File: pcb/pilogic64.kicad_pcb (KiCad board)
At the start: 2 copper layers, 8 parts, among them SW1 RotaryEncoder_Switch, SW2 RotaryEncoder_Switch, U2 Pico

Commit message: Finished cicuit, and I think also finished pcb
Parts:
- added G***: LOGO, LOGO, F.Cu at (178.0, 36.6)
- added G***: LOGO, LOGO, F.Cu at (171.0, 149.3)
- added REF**: KiCad-Logo2_8mm_SilkScreen, Symbol:KiCad-Logo2_8mm_SilkScreen, F.Cu at (112.0, 36.0)
- added REF**: OSHW-Logo_19x20mm_SilkScreen, Symbol:OSHW-Logo_19x20mm_SilkScreen, F.Cu at (114.0, 149.3)
- added U1: ~, Connector_PinHeader_2.54mm:PinHeader_1x04_P2.54mm_Vertical, F.Cu at (139.2, 112.3)
- added U3: pam8403, Library:pam8403, F.Cu at (143.0, 150.0)
- b18650: footprint Battery:BatteryHolder_MPD_BH-18650-PC2 -> Library:18650-PC4
- moved b18650 38.3 mm to (143.0, 80.0)
- moved SD_SPI1 24.7 mm to (117.0, 45.3)
- moved TP4056-18650 24.5 mm to (163.5, 30.4)
- moved MT3608_module_SMT1 22.7 mm to (144.6, 50.3)
- moved SW1 18.9 mm to (104.5, 134.6)
- moved D1 18.7 mm to (117.5, 57.3)
- moved SW2 18.7 mm to (176.5, 134.6)
- moved U2 9.72 mm to (143.2, 127.3), turned to 90 degrees
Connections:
- U2 pad 14: unconnected-(U2-GPIO10-Pad14) -> Net-(U1-SDA)
- U2 pad 15: unconnected-(U2-GPIO11-Pad15) -> Net-(U1-SCL)
- U2 pad 19: unconnected-(U2-GPIO14-Pad19) -> Net-(U2-GPIO14)
- U2 pad 20: unconnected-(U2-GPIO15-Pad20) -> Net-(U2-GPIO15)
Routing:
- net Net-(U2-GPIO7): track 256.8 -> 0.00 mm
- net GND: track 232.8 -> 0.00 mm
- net +3.3V: track 180.0 -> 0.00 mm
- net Net-(D1-K): track 102.2 -> 0.00 mm
- net Net-(SD_SPI1-cs): track 97.6 -> 0.00 mm
- net Net-(SD_SPI1-CLK): track 95.4 -> 0.00 mm
- net Net-(SD_SPI1-MISO): track 92.6 -> 0.00 mm
- net Net-(SD_SPI1-MOSI): track 91.2 -> 0.00 mm
- net Net-(TP4056-18650-B+): track 68.4 -> 0.00 mm
- net Net-(U2-GPIO6): track 43.6 -> 0.00 mm
- net Net-(MT3608_module_SMT1-VIN-): track 26.8 -> 0.00 mm
- net Net-(U2-GPIO8): track 22.9 -> 0.00 mm
- net +5V: track 19.2 -> 0.00 mm
- net Net-(TP4056-18650-B-): track 16.5 -> 0.00 mm
- net Net-(MT3608_module_SMT1-VIN+): track 9.63 -> 0.00 mm
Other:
- board outline added: 90 x 133 mm
- board text added: "Made in Spain"
- board text added: "PiLogic64"
- board text added: "by ThePangel"

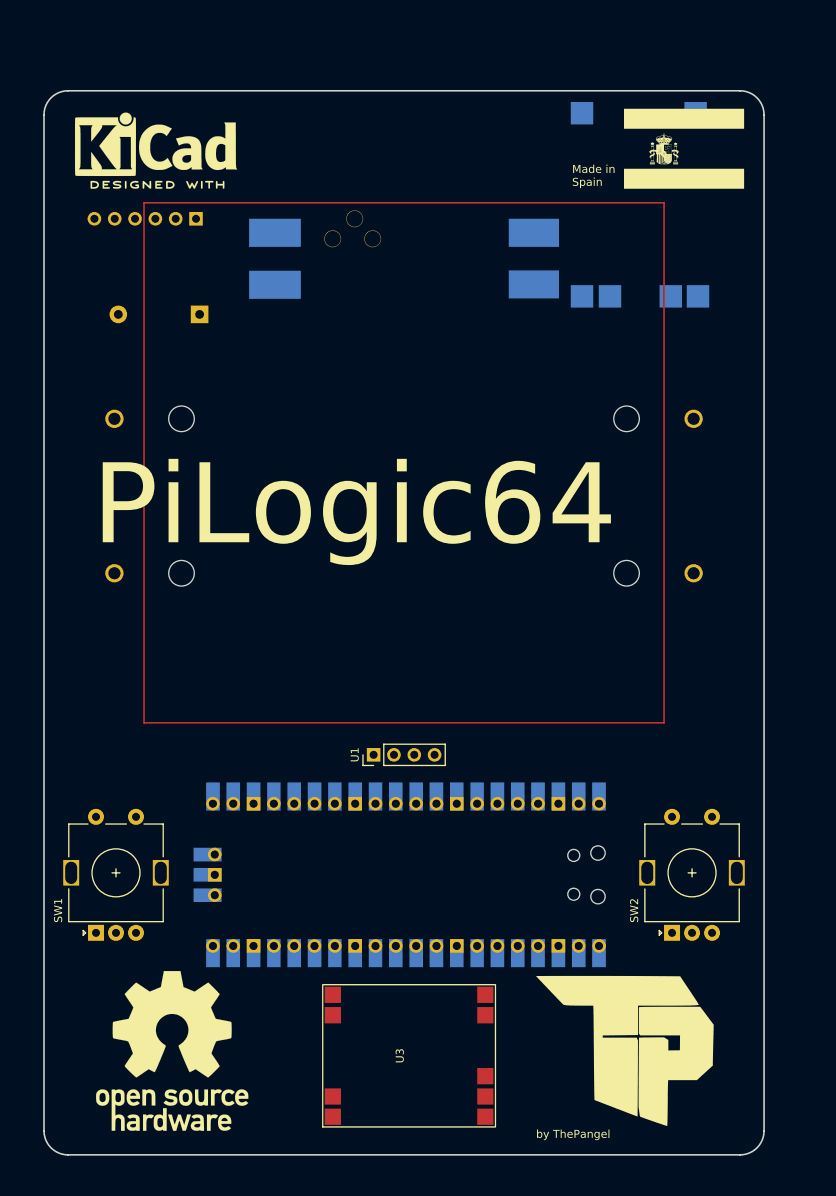
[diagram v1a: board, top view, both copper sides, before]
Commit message: added 3d models and some pcb tweaks
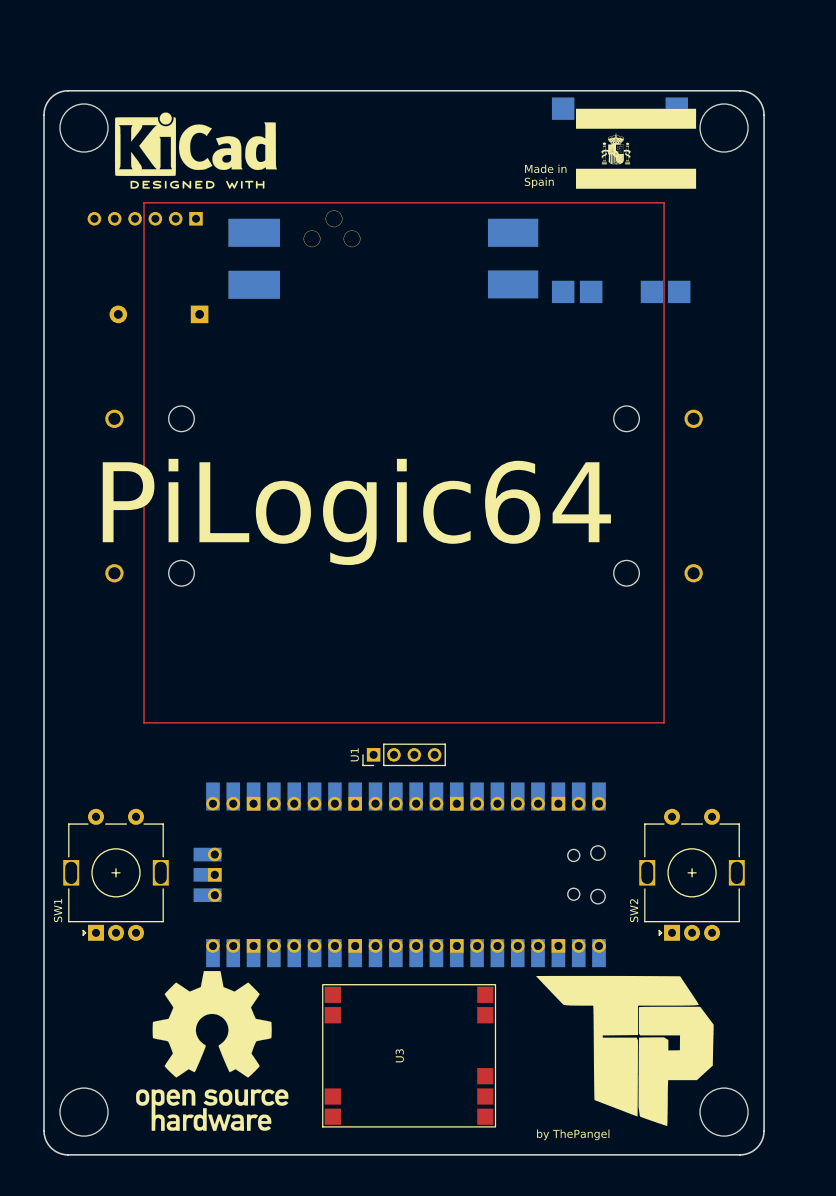
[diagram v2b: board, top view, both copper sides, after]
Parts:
- moved G*** 6.00 mm to (172.0, 36.6)
- moved REF** 5.00 mm to (117.0, 36.0)
- moved REF** 5.00 mm to (119.0, 149.3)
- moved MT3608_module_SMT1 2.59 mm to (142.0, 50.3)
- moved TP4056-18650 2.42 mm to (161.2, 29.9)
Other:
- outline, holes or cut-outs redrawn

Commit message: Finished PCB, added BOM
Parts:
- moved REF** 26.0 mm to (143.0, 34.7)
- moved SD_SPI1 5.01 mm to (115.8, 40.5), turned to 180 degrees
- moved MT3608_module_SMT1 1.15 mm to (143.0, 49.8)
- moved D1 0.70 mm to (117.5, 58.0)
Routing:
- net GND: track 0.00 -> 445.3 mm
- net +3.3V: track 0.00 -> 329.6 mm
- net +5V: track 0.00 -> 178.9 mm
- net Net-(D1-K): track 0.00 -> 125.3 mm
- net Net-(SD_SPI1-cs): track 0.00 -> 123.9 mm, vias 0 -> 1
- net Net-(SD_SPI1-MOSI): track 0.00 -> 113.9 mm, vias 0 -> 1
- net Net-(SD_SPI1-CLK): track 0.00 -> 106.3 mm, vias 0 -> 1
- net Net-(SD_SPI1-MISO): track 0.00 -> 102.1 mm, vias 0 -> 1
- net Net-(TP4056-18650-B+): track 0.00 -> 85.5 mm
- net Net-(U2-GPIO7): track 0.00 -> 58.2 mm
- net Net-(U2-GPIO9): track 0.00 -> 46.3 mm
- net Net-(U2-GPIO15): track 0.00 -> 42.9 mm
- net Net-(U2-GPIO6): track 0.00 -> 38.5 mm
- net Net-(U2-GPIO14): track 0.00 -> 38.2 mm
- net Net-(TP4056-18650-B-): track 0.00 -> 37.3 mm
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
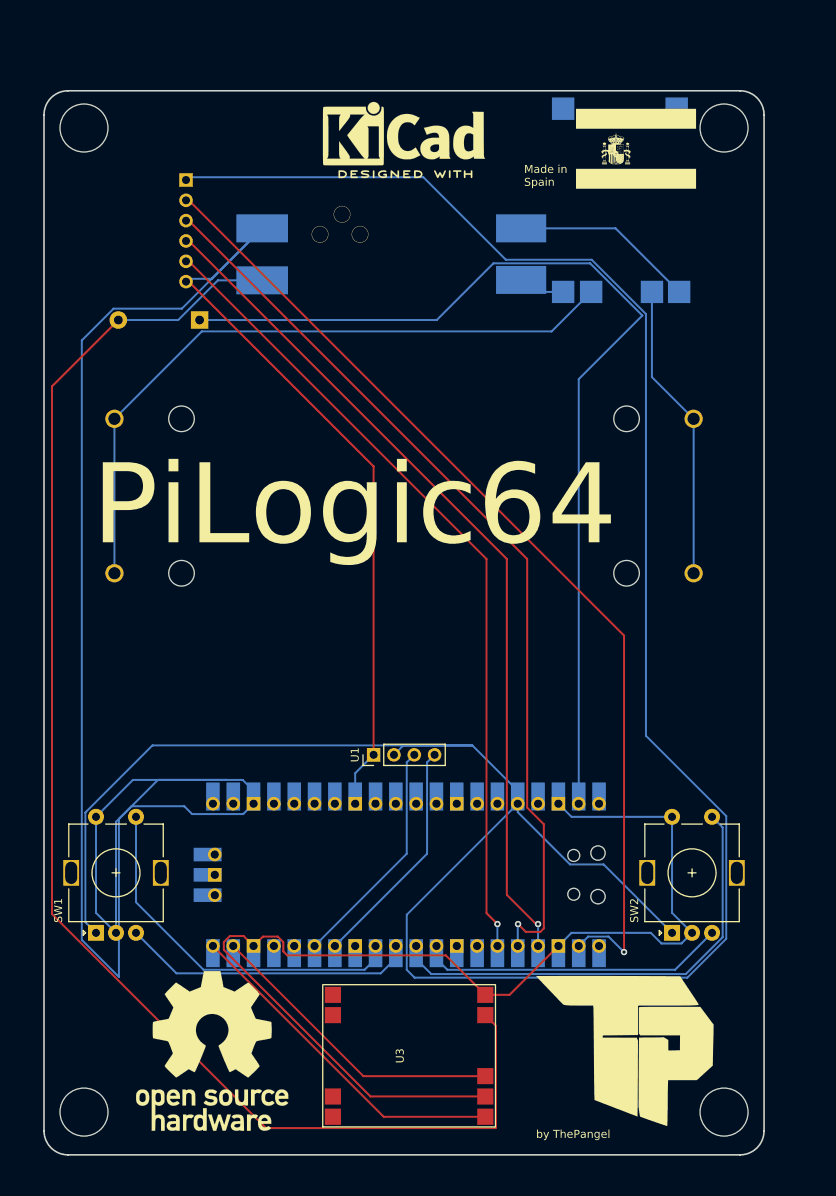
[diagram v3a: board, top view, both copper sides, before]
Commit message: Add new symbols for components and remove lock files; implement main functionality for game selection on microcontroller
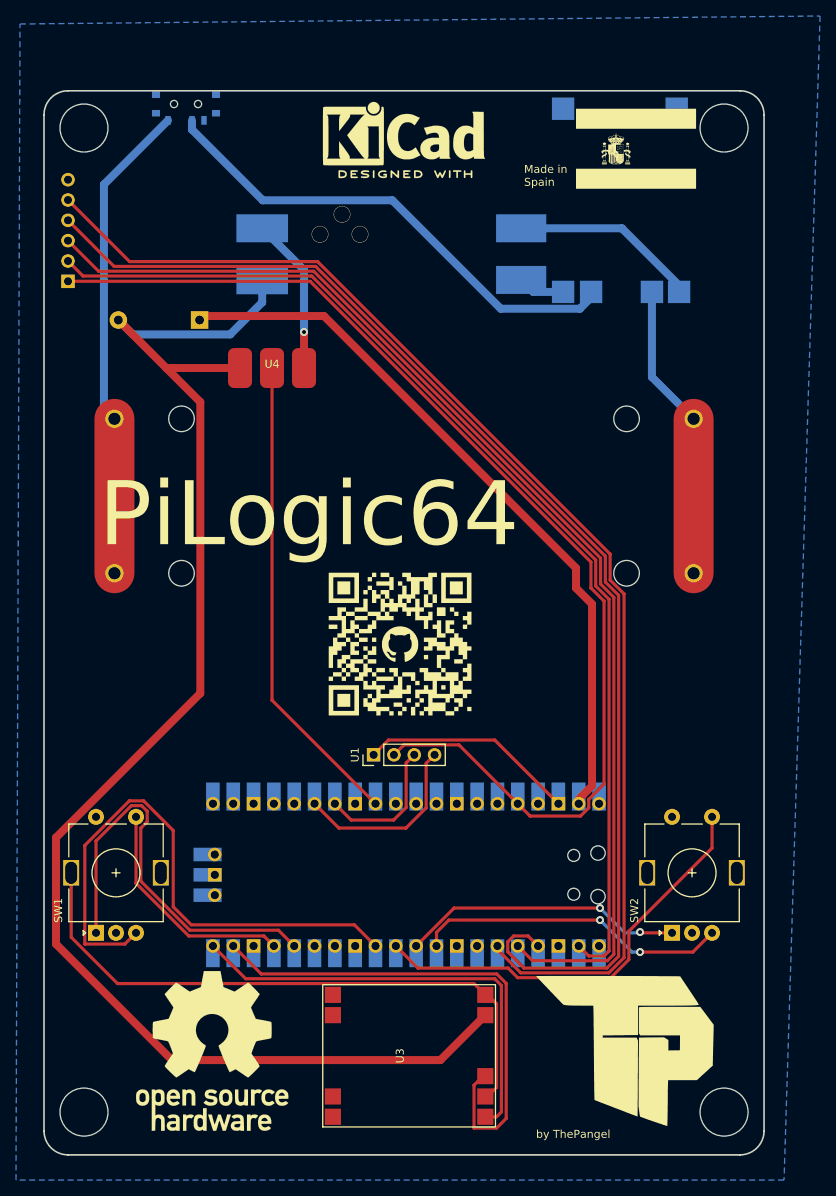
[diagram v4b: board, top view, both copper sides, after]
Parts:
- added G***: LOGO, LOGO, F.Cu at (142.5, 98.5)
- added REF**: Polarity_Center_Positive_6mm_SilkScreen, Symbol:Polarity_Center_Positive_6mm_SilkScreen, B.Cu at (143.0, 70.3)
- added REF**: Polarity_Center_Positive_6mm_SilkScreen, Symbol:Polarity_Center_Positive_6mm_SilkScreen, B.Cu at (143.0, 105.5)
- added REF**: Polarity_Center_Positive_6mm_SilkScreen, Symbol:Polarity_Center_Positive_6mm_SilkScreen, B.Cu at (143.0, 89.7)
- added S1: 450404015514, Library:450404015514, B.Cu at (115.8, 31.0)
- added U4: ~, Library:8x8 MAtrix, F.Cu at (126.5, 64.0)
- moved SD_SPI1 19.4 mm to (101.0, 53.2), turned to 0 degrees
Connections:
- SW1 pad A: +3.3V -> Net-(U2-GPIO12)
- SW1 pad B: Net-(U2-GPIO8) -> Net-(U2-GPIO9)
- SW1 pad MP: (no net) -> GND
- SW1 pad S1: Net-(U2-GPIO9) -> Net-(U2-GPIO13)
- SW2 pad A: +3.3V -> Net-(U2-GPIO7)
- SW2 pad MP: (no net) -> GND
- SW2 pad S1: Net-(U2-GPIO7) -> Net-(U2-GPIO8)
- U2 pad 14: Net-(U1-SDA) -> unconnected-(U2-GPIO10-Pad14)
- U2 pad 15: Net-(U1-SCL) -> unconnected-(U2-GPIO11-Pad15)
- U2 pad 16: unconnected-(U2-GPIO12-Pad16) -> Net-(U2-GPIO12)
- U2 pad 17: unconnected-(U2-GPIO13-Pad17) -> Net-(U2-GPIO13)
- U2 pad 26: unconnected-(U2-GPIO20-Pad26) -> Net-(U1-SDA)
- U2 pad 27: unconnected-(U2-GPIO21-Pad27) -> Net-(U1-SCL)
- U2 pad 29: unconnected-(U2-GPIO22-Pad29) -> Net-(U2-GPIO22)
- U2 pad 42: unconnected-(U2-GND-Pad42) -> GND
- b18650 pad +1: Net-(TP4056-18650-B+) -> Net-(S1-Pad1)
- b18650 pad +2: Net-(TP4056-18650-B+) -> Net-(S1-Pad1)
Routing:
- net GND: track 445.3 -> 123.8 mm, vias 0 -> 1
- net +3.3V: track 329.6 -> 141.1 mm
- net Net-(S1-Pad1): track 0.00 -> 60.5 mm
- net Net-(U2-GPIO22): track 0.00 -> 59.8 mm
- net Net-(SD_SPI1-MISO): track 102.1 -> 155.5 mm, vias 1 -> 0
- net Net-(U2-GPIO12): track 0.00 -> 51.6 mm
- net Net-(SD_SPI1-CLK): track 106.3 -> 156.4 mm, vias 1 -> 0
- net Net-(D1-K): track 125.3 -> 91.3 mm
- net Net-(SD_SPI1-MOSI): track 113.9 -> 146.3 mm, vias 1 -> 0
- net Net-(U2-GPIO13): track 0.00 -> 28.8 mm
- net Net-(U2-GPIO14): track 38.2 -> 64.7 mm
- net Net-(U2-GPIO9): track 46.3 -> 71.1 mm
- net Net-(TP4056-18650-B+): track 85.5 -> 61.6 mm
- net Net-(U2-GPIO7): track 58.2 -> 35.3 mm, vias 0 -> 2
- net Net-(U2-GPIO8): track 36.9 -> 53.9 mm
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- added copper zone on B.Cu, net GND
